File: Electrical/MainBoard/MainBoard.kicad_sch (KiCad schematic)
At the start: 19 parts, among them J1 SNAP Program, SW1 Reset, U1 PIC32MZ2048EFH144-I/PL

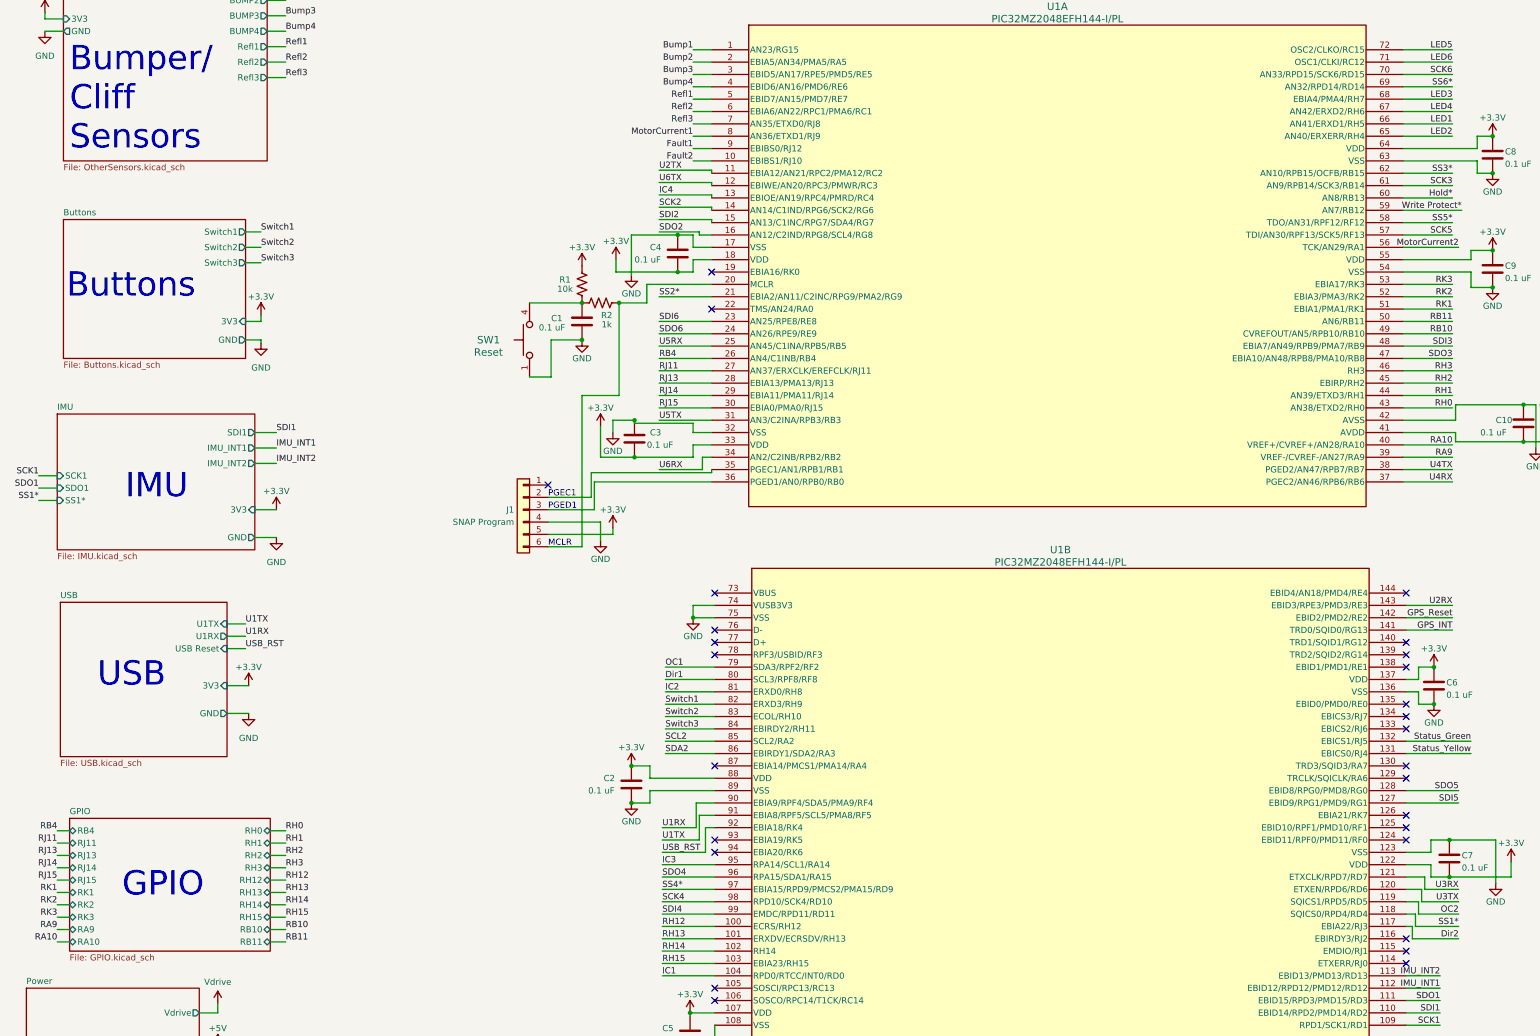
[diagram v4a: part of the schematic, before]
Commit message: First Pass at the routing
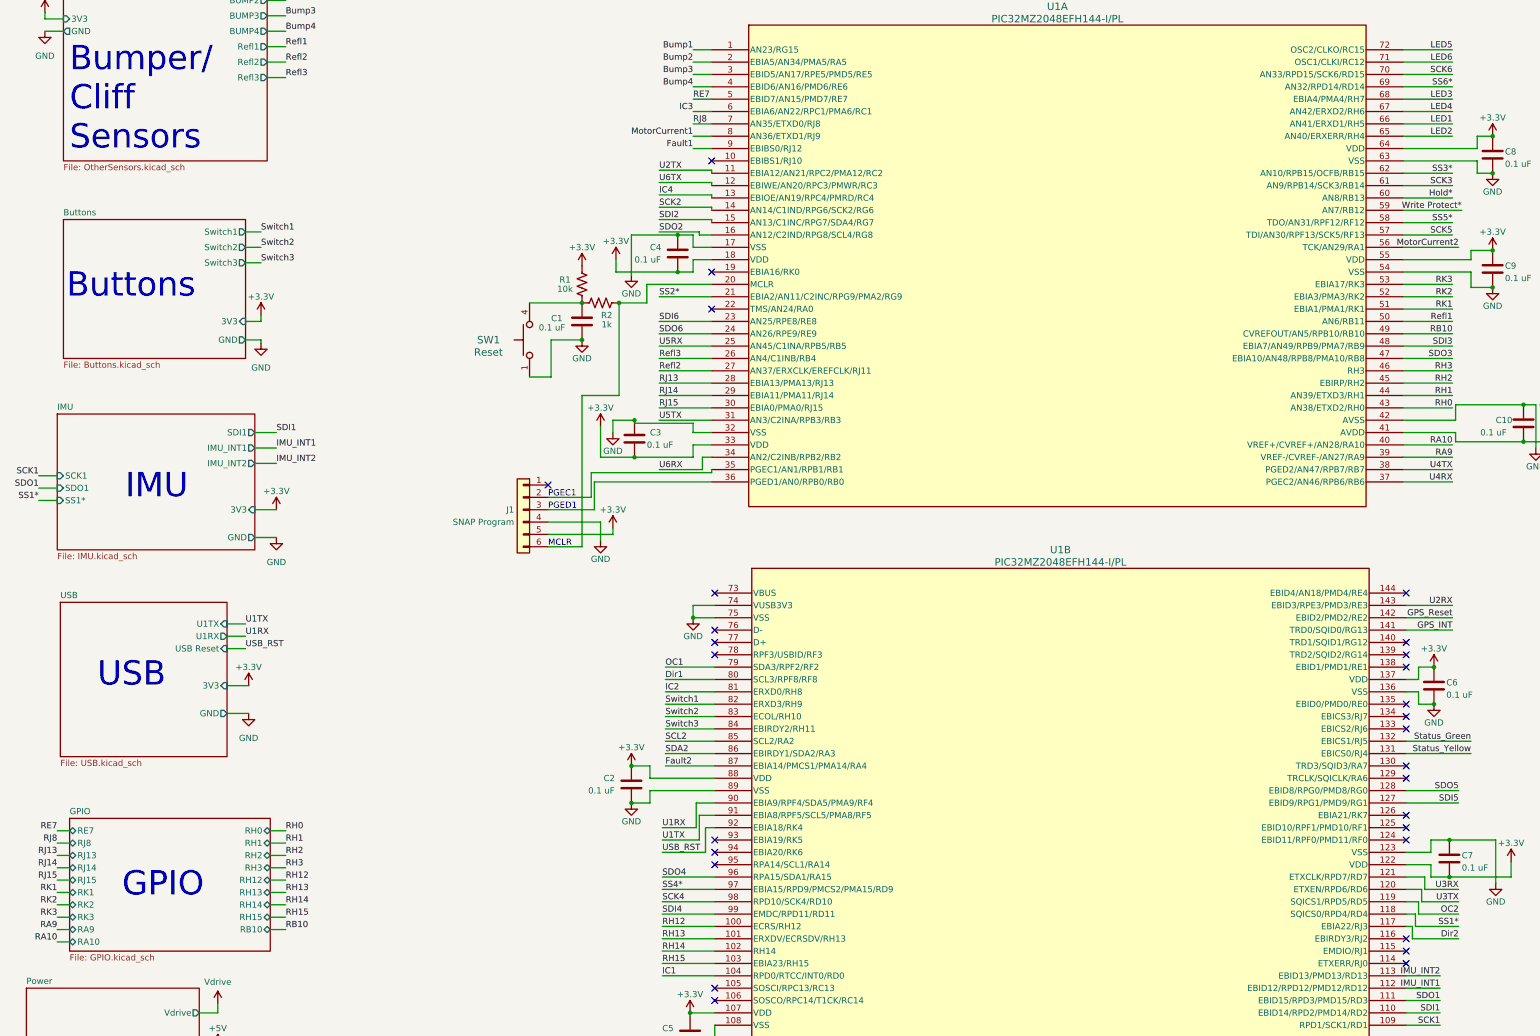
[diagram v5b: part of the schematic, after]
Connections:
- net RB11 is gone; now on net Refl1: U1.50 (AN6/RB11)
- net RB4 is gone; now on net Refl3: U1.26 (AN4/C1INB/RB4)
- net RJ11 is gone; now on net Refl2: U1.27 (AN37/ERXCLK/EREFCLK/RJ11)
- net Fault2: now also U1.87 (EBIA14/PMCS1/PMA14/RA4); no longer U1.10 (EBIBS1/RJ10)
- net IC3: now also U1.6 (EBIA6/AN22/RPC1/PMA6/RC1); no longer U1.95 (RPA14/SCL1/RA14)
- net Refl1: no longer U1.5 (EBID7/AN15/PMD7/RE7)
- net Refl2: no longer U1.6 (EBIA6/AN22/RPC1/PMA6/RC1)
- net Refl3: no longer U1.7 (AN35/ETXD0/RJ8)
- new net RE7: U1.5 (EBID7/AN15/PMD7/RE7)
- new net RJ8: U1.7 (AN35/ETXD0/RJ8)
- no-connect marks 27 -> 28
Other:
- sheet GPIO ports: added RE7, RJ8; removed RB11, RB4, RJ11
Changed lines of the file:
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@@
   (no_connect (at 298.45 172.72))
   (no_connect (at 156.21 203.2))
+  (no_connect (at 155.575 60.96))
   (no_connect (at 298.45 175.26))
   (no_connect (at 156.21 162.56))
@@
   (no_connect (at 156.21 157.48))
   (no_connect (at 298.45 149.86))
-  (no_connect (at 156.21 185.42))
   (no_connect (at 121.92 127.635))
   (no_connect (at 298.45 223.52))
@@
   (no_connect (at 155.575 91.44))
   (no_connect (at 298.45 200.66))
+  (no_connect (at 156.21 205.74))
   (no_connect (at 298.45 185.42))
   (no_connect (at 156.21 233.68))
@@
     (stroke (width 0) (type default))
   )
+  (wire (pts (xy 146.05 185.42) (xy 156.21 185.42))
+    (stroke (width 0) (type default))
+  )
   (wire (pts (xy 155.575 73.025) (xy 155.575 73.66))
     (stroke (width 0) (type default))
@@
     (stroke (width 0) (type default))
   )
-  (wire (pts (xy 64.77 221.615) (xy 67.945 221.615))
-    (stroke (width 0) (type default))
-  )
   (wire (pts (xy 135.255 116.84) (xy 135.255 114.3))
     (stroke (width 0) (type default))
@@
     (stroke (width 0) (type default))
   )
-  (wire (pts (xy 151.765 60.96) (xy 155.575 60.96))
-    (stroke (width 0) (type default))
-  )
   (wire (pts (xy 155.575 62.865) (xy 155.575 63.5))
     (stroke (width 0) (type default))
@@
     (stroke (width 0) (type default))
   )
-  (wire (pts (xy 145.415 205.74) (xy 156.21 205.74))
-    (stroke (width 0) (type default))
-  )
   (wire (pts (xy 131.445 132.715) (xy 121.92 132.715))
     (stroke (width 0) (type default))
@@
     (effects (font (size 1.27 1.27)) (justify right bottom))
   )
-  (label "Refl2" (at 151.765 50.8 180) (fields_autoplaced)
-    (effects (font (size 1.27 1.27)) (justify right bottom))
-  )
   (label "RH12" (at 67.945 208.915 0) (fields_autoplaced)
     (effects (font (size 1.27 1.27)) (justify left bottom))
@@
     (effects (font (size 1.27 1.27)) (justify right bottom))
   )
-  (label "IC3" (at 145.415 205.74 0) (fields_autoplaced)
-    (effects (font (size 1.27 1.27)) (justify left bottom))
-  )
   (label "OC1" (at 146.05 165.1 0) (fields_autoplaced)
     (effects (font (size 1.27 1.27)) (justify left bottom))
@@
     (effects (font (size 1.27 1.27)) (justify right bottom))
   )
-  (label "RB4" (at 20.955 198.755 180) (fields_autoplaced)
-    (effects (font (size 1.27 1.27)) (justify right bottom))
-  )
   (label "SDO6" (at 144.78 96.52 0) (fields_autoplaced)
     (effects (font (size 1.27 1.27)) (justify left bottom))
   )
+  (label "RE7" (at 151.765 48.26 0) (fields_autoplaced)
+    (effects (font (size 1.27 1.27)) (justify left bottom))
+  )
   (label "SS3*" (at 359.41 113.03 180) (fields_autoplaced)
     (effects (font (size 1.27 1.27)) (justify right bottom))
@@
     (effects (font (size 1.27 1.27)) (justify right bottom))
   )
+  (label "RJ8" (at 20.955 201.295 180) (fields_autoplaced)
+    (effects (font (size 1.27 1.27)) (justify right bottom))
+  )
   (label "SS5*" (at 307.975 73.66 180) (fields_autoplaced)
     (effects (font (size 1.27 1.27)) (justify right bottom))
@@
     (effects (font (size 1.27 1.27)) (justify right bottom))
   )
-  (label "RB11" (at 307.975 93.98 180) (fields_autoplaced)
-    (effects (font (size 1.27 1.27)) (justify right bottom))
-  )
   (label "U3RX" (at 408.305 93.345 0) (fields_autoplaced)
     (effects (font (size 1.27 1.27)) (justify left bottom))
@@
     (effects (font (size 1.27 1.27)) (justify right bottom))
   )
-  (label "RJ11" (at 144.78 104.14 0) (fields_autoplaced)
-    (effects (font (size 1.27 1.27)) (justify left bottom))
-  )
   (label "RH15" (at 67.945 216.535 0) (fields_autoplaced)
     (effects (font (size 1.27 1.27)) (justify left bottom))
@@
     (effects (font (size 1.27 1.27)) (justify right bottom))
   )
-  (label "RB11" (at 67.945 221.615 0) (fields_autoplaced)
+  (label "Fault2" (at 146.05 185.42 0) (fields_autoplaced)
     (effects (font (size 1.27 1.27)) (justify left bottom))
   )
@@
     (effects (font (size 1.27 1.27)) (justify left bottom))
   )
-  (label "RJ11" (at 20.955 201.295 180) (fields_autoplaced)
-    (effects (font (size 1.27 1.27)) (justify right bottom))
-  )
   (label "U2RX" (at 368.935 33.02 180) (fields_autoplaced)
     (effects (font (size 1.27 1.27)) (justify right bottom))
@@
     (effects (font (size 1.27 1.27)) (justify right bottom))
   )
+  (label "RE7" (at 20.955 198.755 180) (fields_autoplaced)
+    (effects (font (size 1.27 1.27)) (justify right bottom))
+  )
   (label "Bump2" (at 151.765 40.64 180) (fields_autoplaced)
     (effects (font (size 1.27 1.27)) (justify right bottom))
@@
     (effects (font (size 1.27 1.27)) (justify left bottom))
   )
+  (label "RJ8" (at 151.765 53.34 0) (fields_autoplaced)
+    (effects (font (size 1.27 1.27)) (justify left bottom))
+  )
   (label "Bump4" (at 151.765 45.72 180) (fields_autoplaced)
     (effects (font (size 1.27 1.27)) (justify right bottom))
@@
     (effects (font (size 1.27 1.27)) (justify left bottom))
   )
-  (label "Refl1" (at 151.765 48.26 180) (fields_autoplaced)
-    (effects (font (size 1.27 1.27)) (justify right bottom))
-  )
   (label "Switch2" (at 146.05 175.26 0) (fields_autoplaced)
     (effects (font (size 1.27 1.27)) (justify left bottom))
@@
     (effects (font (size 1.27 1.27)) (justify left bottom))
   )
+  (label "Refl2" (at 144.78 104.14 0) (fields_autoplaced)
+    (effects (font (size 1.27 1.27)) (justify left bottom))
+  )
   (label "U1RX" (at 59.69 158.75 0) (fields_autoplaced)
     (effects (font (size 1.27 1.27)) (justify left bottom))
@@
     (effects (font (size 1.27 1.27)) (justify right bottom))
   )
-  (label "RB4" (at 144.78 101.6 0) (fields_autoplaced)
-    (effects (font (size 1.27 1.27)) (justify left bottom))
-  )
-  (label "Fault2" (at 151.765 60.96 180) (fields_autoplaced)
-    (effects (font (size 1.27 1.27)) (justify right bottom))
-  )
   (label "RH1" (at 67.945 201.295 0) (fields_autoplaced)
     (effects (font (size 1.27 1.27)) (justify left bottom))
@@
     (effects (font (size 1.27 1.27)) (justify left bottom))
   )
+  (label "IC3" (at 151.765 50.8 180) (fields_autoplaced)
+    (effects (font (size 1.27 1.27)) (justify right bottom))
+  )
   (label "Bump1" (at 151.765 38.1 180) (fields_autoplaced)
     (effects (font (size 1.27 1.27)) (justify right bottom))
@@
     (effects (font (size 1.27 1.27)) (justify right bottom))
   )
+  (label "Refl1" (at 307.975 93.98 180) (fields_autoplaced)
+    (effects (font (size 1.27 1.27)) (justify right bottom))
+  )
   (label "LED1" (at 359.41 59.69 180) (fields_autoplaced)
     (effects (font (size 1.27 1.27)) (justify right bottom))
@@
     (effects (font (size 1.27 1.27)) (justify right bottom))
   )
-  (label "Refl3" (at 151.765 53.34 180) (fields_autoplaced)
-    (effects (font (size 1.27 1.27)) (justify right bottom))
-  )
   (label "SDI1" (at 66.04 116.84 0) (fields_autoplaced)
     (effects (font (size 1.27 1.27)) (justify left bottom))
@@
     (effects (font (size 1.27 1.27)) (justify right bottom))
   )
+  (label "Refl3" (at 144.78 101.6 0) (fields_autoplaced)
+    (effects (font (size 1.27 1.27)) (justify left bottom))
+  )
   (label "SDO4" (at 145.415 208.28 0) (fields_autoplaced)
     (effects (font (size 1.27 1.27)) (justify left bottom))
@@
       (effects (font (size 1.27 1.27)) (justify right))
     )
-    (pin "RB11" bidirectional (at 64.77 221.615 0)
-      (effects (font (size 1.27 1.27)) (justify right))
-    )
     (pin "RK1" bidirectional (at 23.495 211.455 180)
       (effects (font (size 1.27 1.27)) (justify left))
@@
       (effects (font (size 1.27 1.27)) (justify left))
     )
-    (pin "RB4" bidirectional (at 23.495 198.755 180)
+    (pin "RJ14" bidirectional (at 23.495 206.375 180)
       (effects (font (size 1.27 1.27)) (justify left))
     )
-    (pin "RJ11" bidirectional (at 23.495 201.295 180)
+    (pin "RJ13" bidirectional (at 23.495 203.835 180)
       (effects (font (size 1.27 1.27)) (justify left))
     )
-    (pin "RJ14" bidirectional (at 23.495 206.375 180)
+    (pin "RJ15" bidirectional (at 23.495 208.915 180)
       (effects (font (size 1.27 1.27)) (justify left))
     )
-    (pin "RJ13" bidirectional (at 23.495 203.835 180)
+    (pin "RJ8" bidirectional (at 23.495 201.295 180)
       (effects (font (size 1.27 1.27)) (justify left))
     )
-    (pin "RJ15" bidirectional (at 23.495 208.915 180)
+    (pin "RE7" bidirectional (at 23.495 198.755 180)
       (effects (font (size 1.27 1.27)) (justify left))
     )

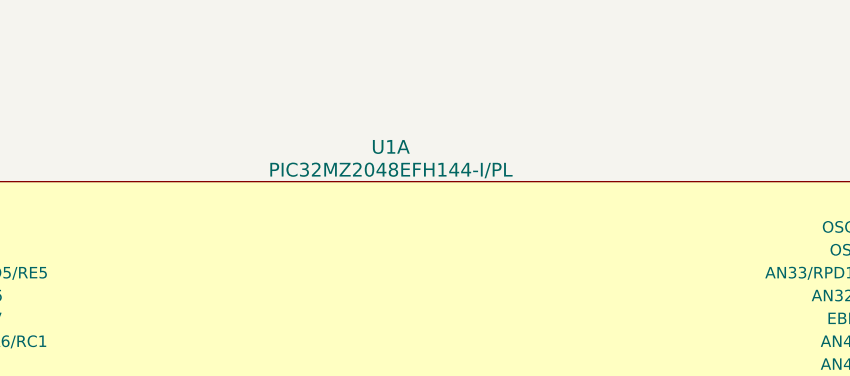
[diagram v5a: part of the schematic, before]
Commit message: Move reflectlive sensors to own schematic
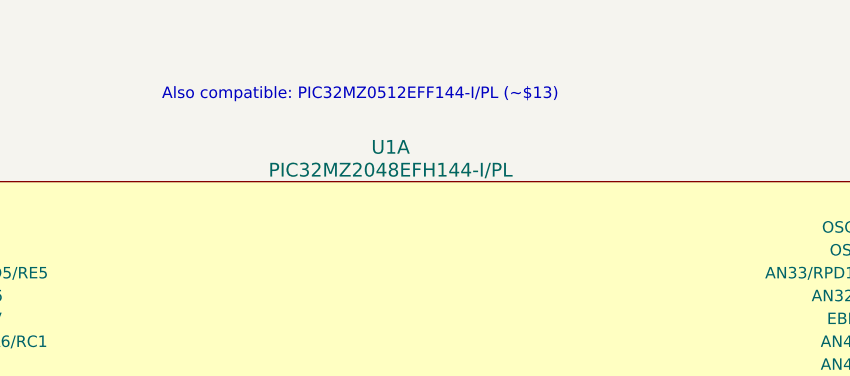
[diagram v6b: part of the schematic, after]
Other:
- note added: "Also compatible: PIC32MZ0512EFF144-I/PL (~$13)"
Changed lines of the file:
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@@
+    (effects (font (size 1.27 1.27)) (justify left bottom))
+  )
+  (text "Also compatible: PIC32MZ0512EFF144-I/PL (~$13)" (at 201.295 24.13 0)
     (effects (font (size 1.27 1.27)) (justify left bottom))
   )

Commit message: Add some final touches
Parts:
- H1, H2, H3, H4: now left out of the parts list
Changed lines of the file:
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@@
   )
   (symbol (lib_id "Lab_3:MountingHole") (at 285.75 253.365 0) (unit 1)
-    (in_bom yes) (on_board yes) (dnp no) (fields_autoplaced)
+    (in_bom no) (on_board yes) (dnp no) (fields_autoplaced)
     (property "Reference" "H3" (at 288.925 252.095 0)
       (effects (font (size 1.27 1.27)) (justify left))
@@
   )
   (symbol (lib_id "Lab_3:MountingHole") (at 263.525 253.365 0) (unit 1)
-    (in_bom yes) (on_board yes) (dnp no) (fields_autoplaced)
+    (in_bom no) (on_board yes) (dnp no) (fields_autoplaced)
     (property "Reference" "H1" (at 266.7 252.095 0)
       (effects (font (size 1.27 1.27)) (justify left))
@@
   )
   (symbol (lib_id "Lab_3:MountingHole") (at 285.75 262.255 0) (unit 1)
-    (in_bom yes) (on_board yes) (dnp no) (fields_autoplaced)
+    (in_bom no) (on_board yes) (dnp no) (fields_autoplaced)
     (property "Reference" "H4" (at 288.925 260.985 0)
       (effects (font (size 1.27 1.27)) (justify left))
@@
   )
   (symbol (lib_id "Lab_3:MountingHole") (at 263.525 262.89 0) (unit 1)
-    (in_bom yes) (on_board yes) (dnp no) (fields_autoplaced)
+    (in_bom no) (on_board yes) (dnp no) (fields_autoplaced)
     (property "Reference" "H2" (at 266.7 261.62 0)
       (effects (font (size 1.27 1.27)) (justify left))

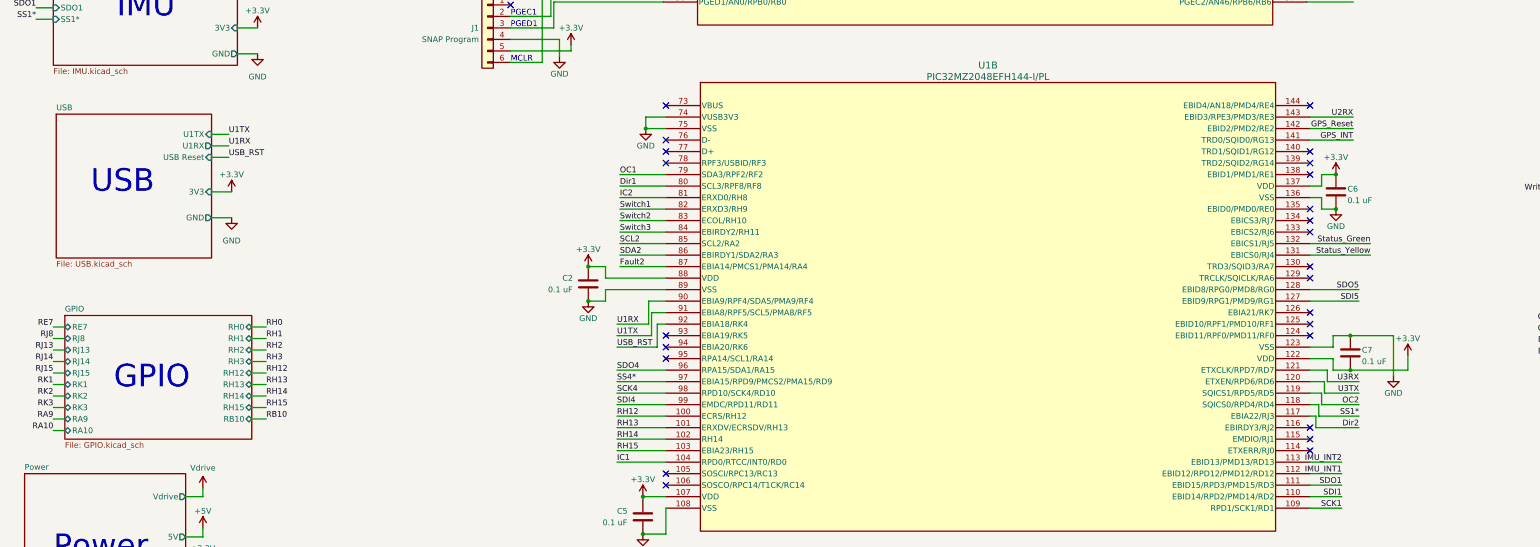
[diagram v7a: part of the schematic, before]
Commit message: Finish final board design for Rev 0.1 Main board and reflective Sensor. Created Gerbers.
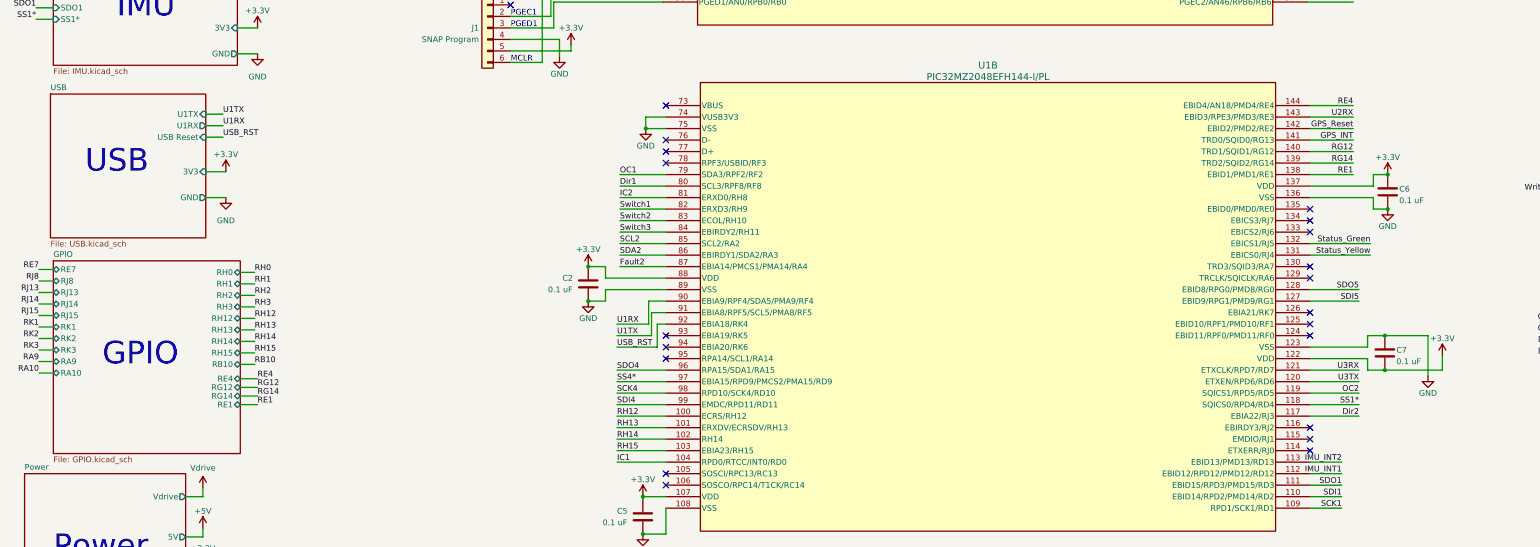
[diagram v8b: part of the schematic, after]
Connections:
- net RE1: now reaches U1.138 (EBID1/PMD1/RE1)
- net RG14: now reaches U1.139 (TRD2/SQID2/RG14)
- net RG12: now reaches U1.140 (TRD1/SQID1/RG12)
- net RE4: now reaches U1.144 (EBID4/AN18/PMD4/RE4)
- no-connect marks 28 -> 24
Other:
- sheet GPIO ports: added RE1, RE4, RG12, RG14; removed none
- moved on the sheet: C6, C7
